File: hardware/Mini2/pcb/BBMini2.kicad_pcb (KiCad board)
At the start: 4 copper layers, 100 x 62 mm, 80 parts, among them J1 Barrel_Jack_Switch, J2 USB_B_Mini, J3 Display, Q1 MBT2222ADW1T1, SW1 SW_SPDT, SW2 SW_Push, SW3 SW_Push, SW4 SW_Push, U1 ESP8266EX, U2 AT25SF081-SSHF-X, U3 AP2112K-3.3, U4 CP2104, U5 MCP3208, U6 LM2576S-5, U7 REF02AU, Y1 ABM8-26.000MHZ-10-1-U-T

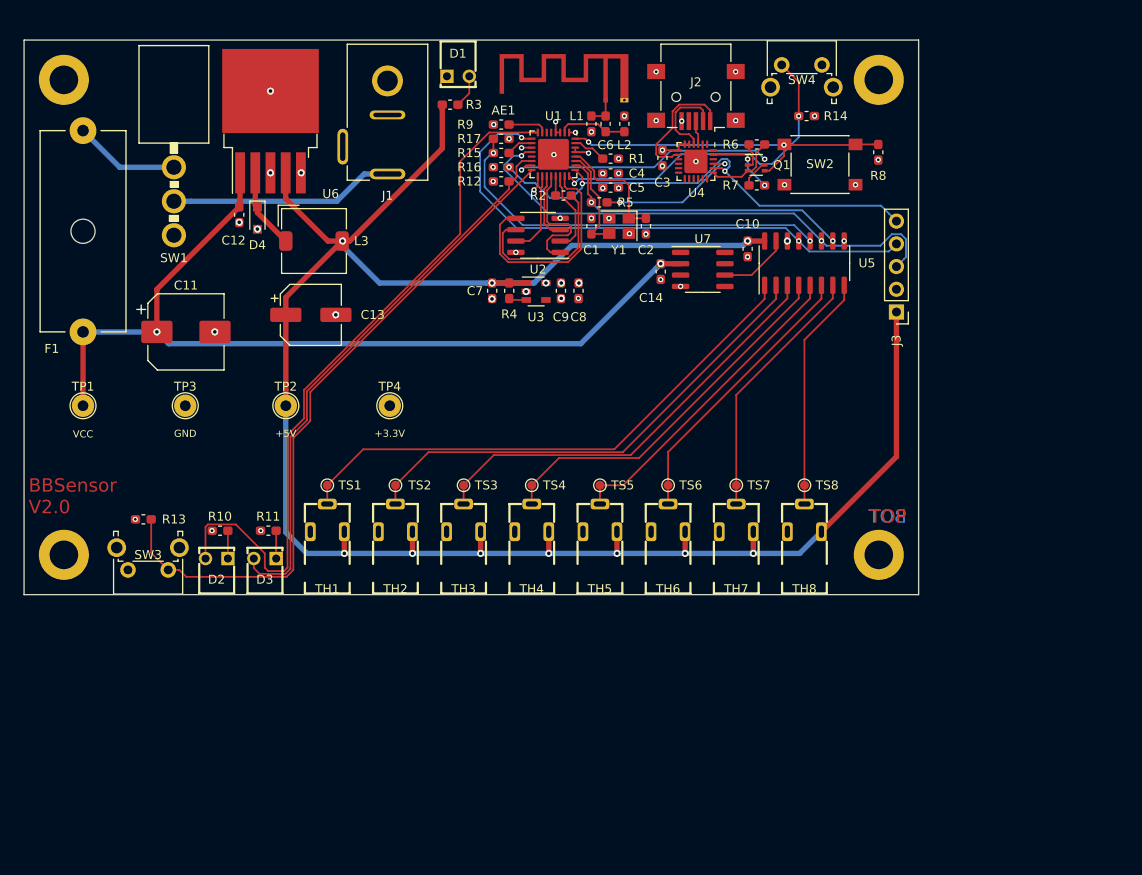
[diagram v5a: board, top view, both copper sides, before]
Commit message: feat: BBMini2 - experimental ESP8266 PCB (SMD)
* update Mini2 with current SDK

Issue #23
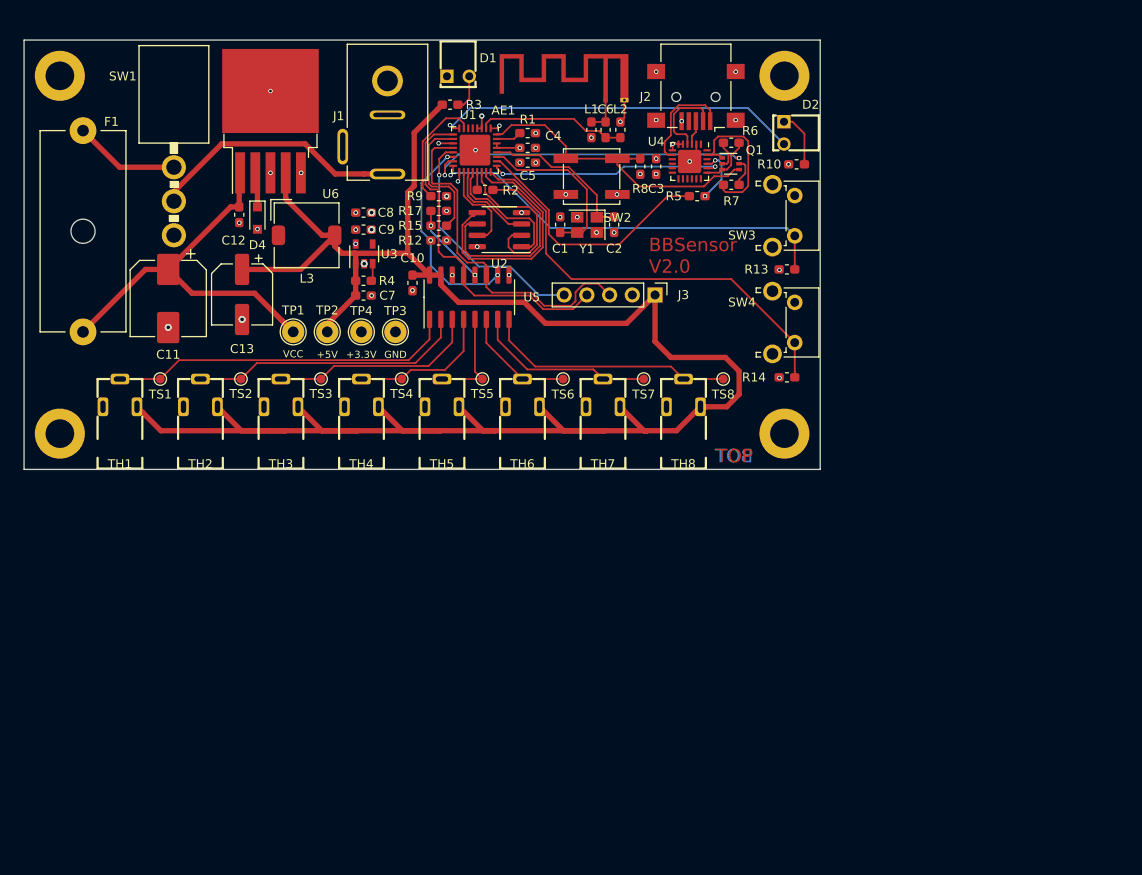
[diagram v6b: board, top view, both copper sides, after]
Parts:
- removed C14: 100n, Capacitor_SMD:C_0603_1608Metric_Pad1.05x0.95mm_HandSolder
- removed D3: LED_GREEN, VCC:5600F
- removed R11: 140, Resistor_SMD:R_0603_1608Metric_Pad1.05x0.95mm_HandSolder
- removed R16: 4k7, Resistor_SMD:R_0603_1608Metric_Pad1.05x0.95mm_HandSolder
- removed U7: REF02AU, Package_SO:SOIC-8_3.9x4.9mm_P1.27mm
- D2: value LED_RED -> LED
- SW2: footprint Button_Switch_SMD:SW_Push_1P1T_NO_6x6mm_H9.5mm -> Button_Switch_SMD:SW_SPST_EVPBF
- moved D2 84.9 mm to (103.9, 25.4), turned to 270 degrees
- moved SW3 81.6 mm to (101.2, 32.4), turned to 270 degrees
- moved R13 77.2 mm to (100.3, 40.6), turned to 180 degrees
- moved R10 76.4 mm to (101.4, 28.9), turned to 180 degrees
- moved U5 37.7 mm to (64.8, 43.8)
- moved C10 37.7 mm to (58.4, 42.1)
- moved R14 29.3 mm to (100.3, 52.7)
- moved TH1 27.1 mm to (25.7, 62.9)
- moved J3 27.1 mm to (85.5, 43.5), turned to 270 degrees
- moved R8 26.7 mm to (83.9, 29.1), turned to 270 degrees
- moved SW4 26.6 mm to (101.2, 44.3), turned to 270 degrees
- moved TH2 25.9 mm to (34.7, 62.9)
- moved C8 25.6 mm to (52.9, 34.3), turned to 180 degrees
- moved SW2 25.6 mm to (78.4, 30.3), turned to 0 degrees
- moved TP1 24.9 mm to (45.1, 47.6)
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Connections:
- net /ESP8266EX/GPIO13 renamed /ESP8266EX/MOSI
- net /ESP8266EX/GPIO14 renamed /ESP8266EX/SCLK
- net /IO/MISO renamed /ESP8266EX/MISO
- J3 pad 5: /ESP8266EX/GPIO1_TXD -> /ESP8266EX/GPIO15
- R10 pad 1: +3V3 -> Net-(D2-Pad1)
- R10 pad 2: Net-(D2-Pad1) -> +3V3
- R12 pad 1: +3V3 -> /ESP8266EX/CS1
- R12 pad 2: /ESP8266EX/GPIO2 -> +3V3
- R13 pad 1: GND -> /ESP8266EX/GPIO4
- R13 pad 2: /ESP8266EX/GPIO4 -> GND
- R14 pad 1: GND -> /ESP8266EX/GPIO5
- R14 pad 2: /ESP8266EX/GPIO5 -> GND
- R5 pad 2: /IO/CS1 -> /ESP8266EX/GPIO3_RXD
- R8 pad 1: +3V3 -> /ESP8266EX/~RST
- R8 pad 2: /ESP8266EX/~RST -> +3V3
- R9 pad 1: +3V3 -> /ESP8266EX/EN
- R9 pad 2: /ESP8266EX/EN -> +3V3
- SW2 pad 1: GND -> /ESP8266EX/~RST
- SW2 pad 2: /ESP8266EX/~RST -> GND
- SW3 pad 1: /ESP8266EX/GPIO4 -> +3V3
- SW3 pad 2: +3V3 -> /ESP8266EX/GPIO4
- SW4 pad 1: /ESP8266EX/GPIO5 -> +3V3
- SW4 pad 2: +3V3 -> /ESP8266EX/GPIO5
- U1 pad 13: Net-(U1-Pad13) -> /ESP8266EX/GPIO15
- U1 pad 14: /ESP8266EX/GPIO2 -> /ESP8266EX/CS1
- U1 pad 26: /IO/CS1 -> /ESP8266EX/GPIO3_RXD
- U5 pad 10: /IO/CS1 -> /ESP8266EX/CS1
- U5 pad 15: /Temperature/VREF -> +5V
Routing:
- net /ESP8266EX/GPIO2: track 63.3 -> 0.00 mm
- net VCC: track 100.9 -> 44.0 mm, vias 2 -> 0
- net /ESP8266EX/GPIO16: track 79.5 -> 41.0 mm, vias 0 -> 1
- net /ESP8266EX/MISO: track 44.8 -> 9.22 mm
- net /IO/CS1: track 34.0 -> 0.00 mm, vias 2 -> 0
- net /ESP8266EX/GPIO4: track 76.8 -> 46.4 mm, vias 0 -> 1
- net /ESP8266EX/GPIO3_RXD: track 0.00 -> 29.2 mm
- net /ESP8266EX/GPIO1_TXD: track 54.3 -> 26.3 mm, vias 3 -> 2
- net /ESP8266EX/GPIO15: track 0.00 -> 26.6 mm, vias 0 -> 1
- net /Temperature/SIGNAL4: track 42.1 -> 16.3 mm
- net /Temperature/SIGNAL3: track 48.4 -> 23.4 mm
- net /Temperature/SIGNAL5: track 35.7 -> 11.5 mm
- net /Temperature/SIGNAL2: track 54.8 -> 30.8 mm
- net /ESP8266EX/CS1: track 0.00 -> 23.2 mm, vias 0 -> 3
- net /ESP8266EX/SCLK: track 60.9 -> 38.0 mm, vias 2 -> 0
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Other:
- board size 100 x 62 mm -> 89 x 48 mm
- net class Default: via_dia 0.6 -> 0.5
